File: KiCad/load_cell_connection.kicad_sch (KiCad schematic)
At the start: 10 parts, among them J2 Conn_01x04

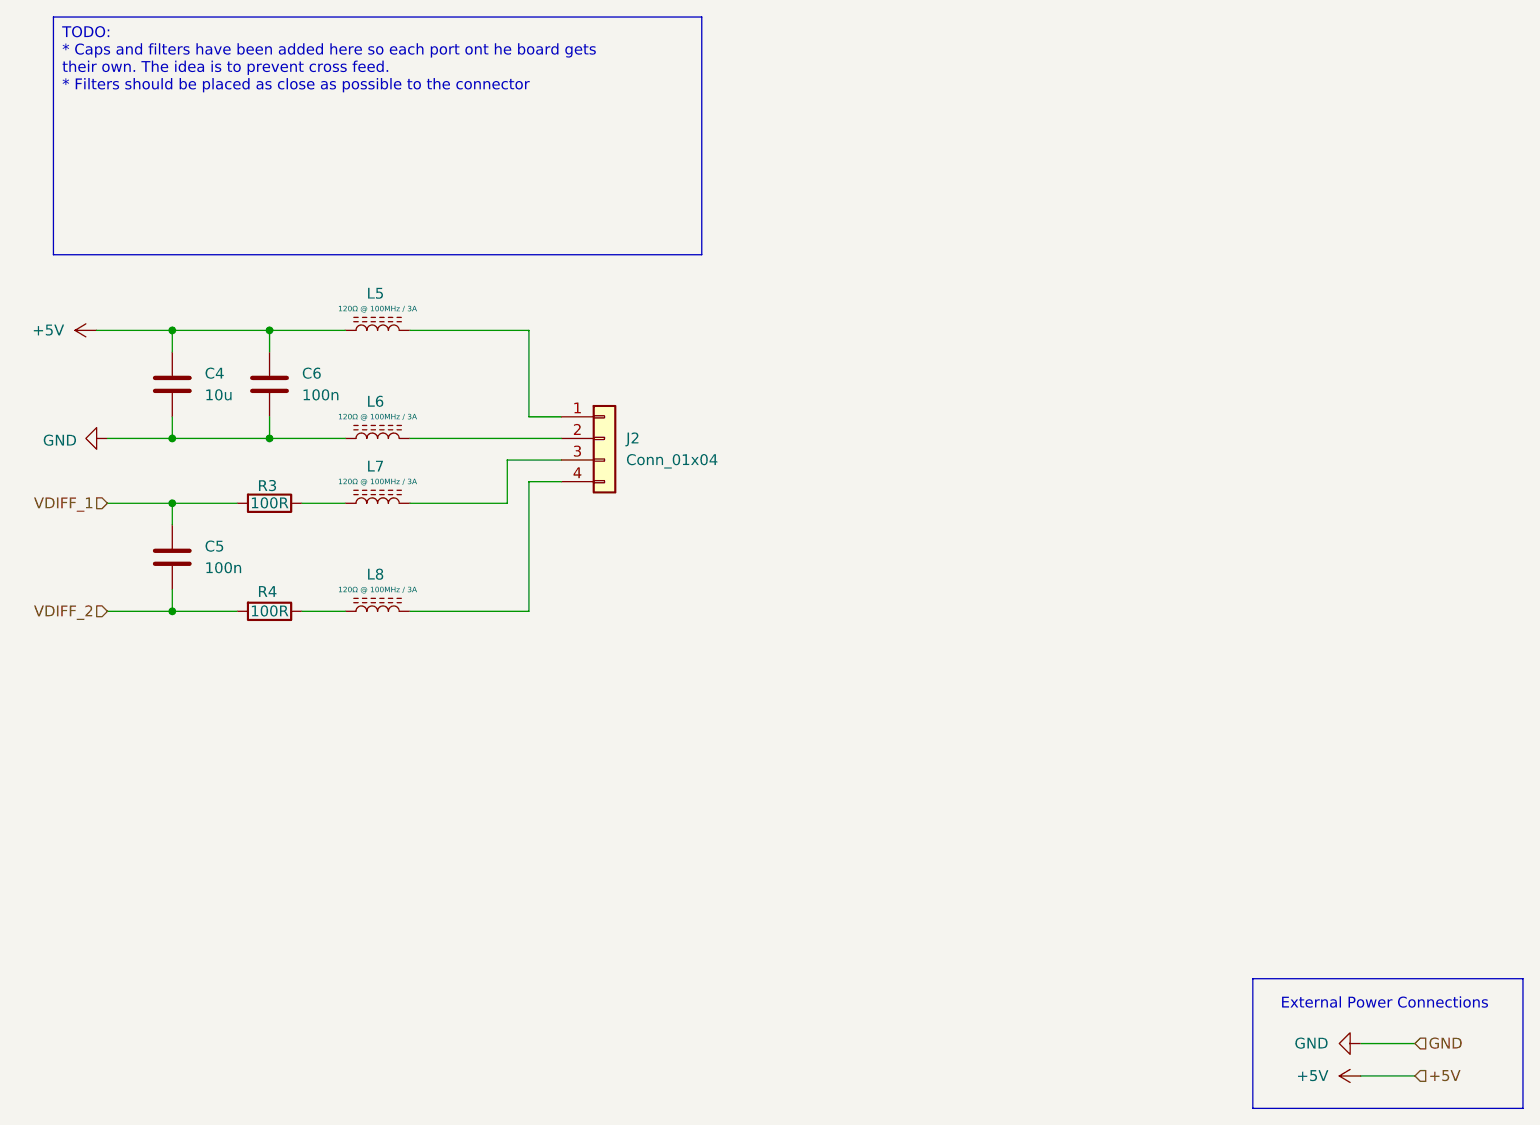
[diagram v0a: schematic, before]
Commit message: Use 12V Power
* Use 12 V Power
* Update to an F103 processor with better compatibility with Katapult
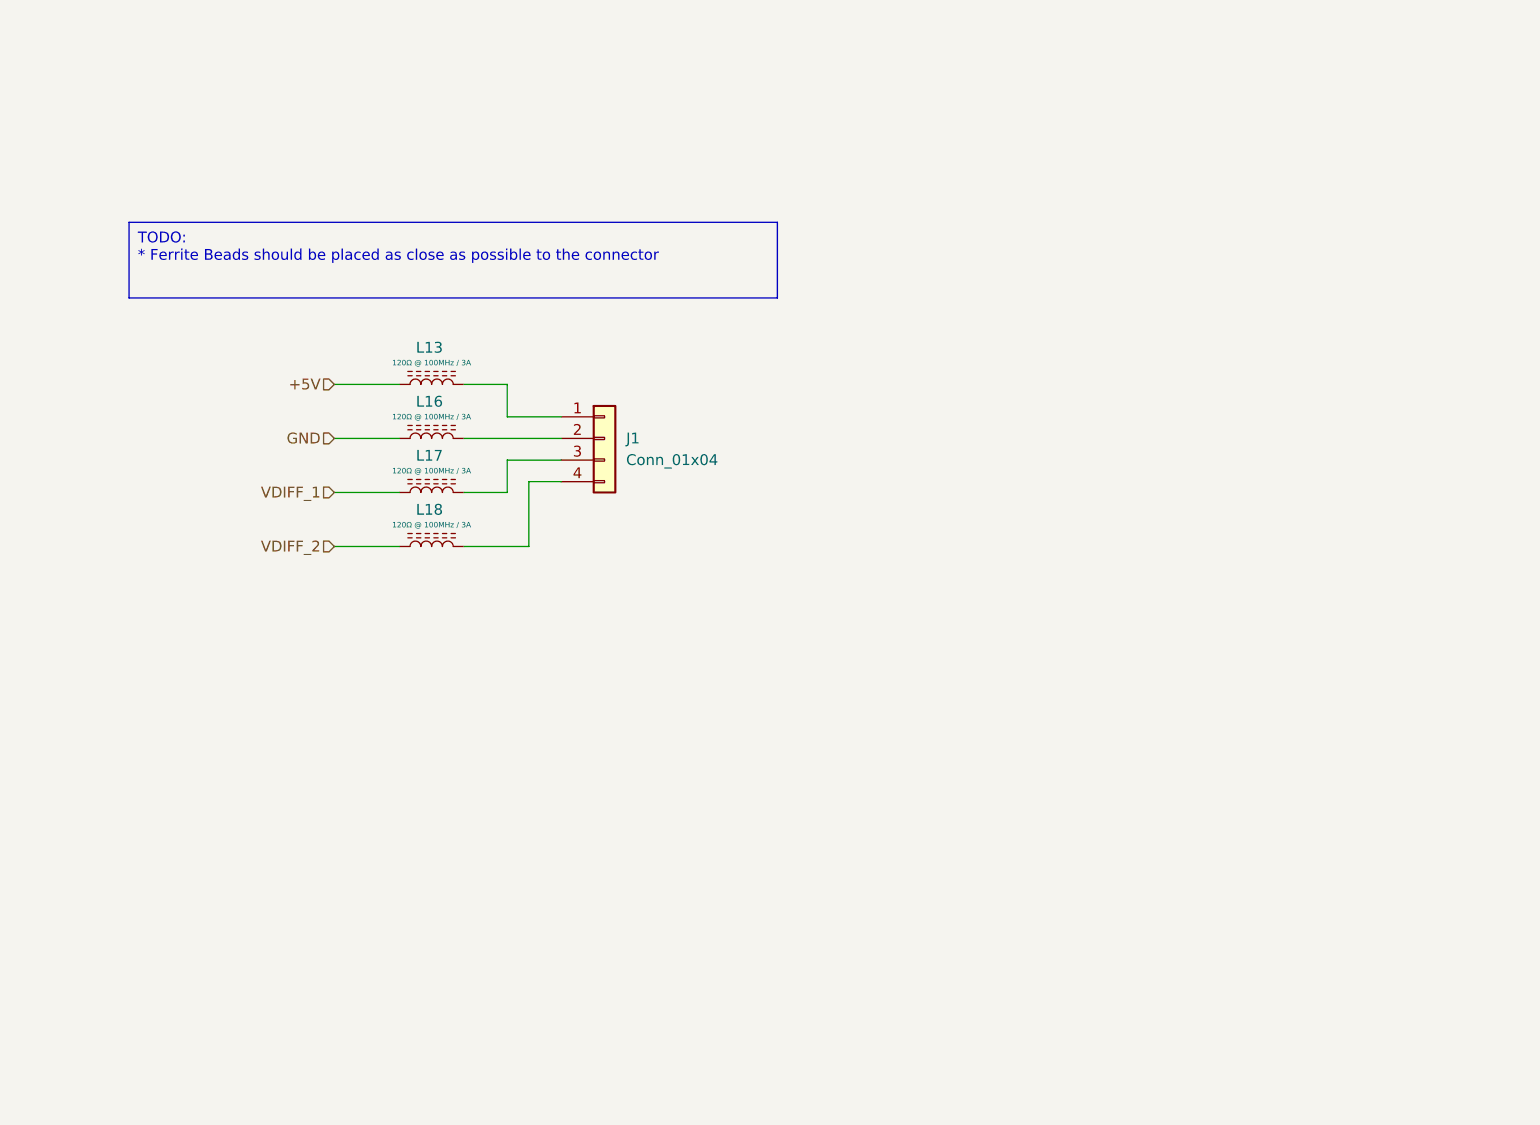
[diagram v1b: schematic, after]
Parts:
- removed C4: 10u, symbol Device:C
- removed C5, C6: 100n, symbol Device:C
- removed R3, R4: 100R, symbol Device:R
- J1: renamed from J2; footprint (none) -> Connector_JST:JST_XH_S4B-XH-A-1_1x04_P2.50mm_Horizontal
- L13: renamed from L5; footprint (none) -> Inductor_SMD:L_0603_1608Metric_Pad1.05x0.95mm_HandSolder
- L16: renamed from L6; footprint (none) -> Inductor_SMD:L_0603_1608Metric_Pad1.05x0.95mm_HandSolder
- L17: renamed from L7; footprint (none) -> Inductor_SMD:L_0603_1608Metric_Pad1.05x0.95mm_HandSolder
- L18: renamed from L8; footprint (none) -> Inductor_SMD:L_0603_1608Metric_Pad1.05x0.95mm_HandSolder
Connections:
- net VDIFF_1: now also L17.1
- net VDIFF_2: now also L18.1
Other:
- note removed: "External Power Connections"
- moved on the sheet: L13, L16, L17, L18

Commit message: Update 5V Power Stage
* Update the 5V power stage based on the recommendations from TI.
* Updated standard passive footprint to 0805 hand solder configuration
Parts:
- L13, L16, L17, L18: footprint Inductor_SMD:L_0603_1608Metric_Pad1.05x0.95mm_HandSolder -> Inductor_SMD:L_0805_2012Metric_Pad1.05x1.20mm_HandSolder
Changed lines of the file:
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@@
 			)
 		)
-		(property "Footprint" "Inductor_SMD:L_0603_1608Metric_Pad1.05x0.95mm_HandSolder"
+		(property "Footprint" "Inductor_SMD:L_0805_2012Metric_Pad1.05x1.20mm_HandSolder"
 			(at 153.67 97.79 0)
 			(effects
@@
 			)
 		)
-		(property "Footprint" "Inductor_SMD:L_0603_1608Metric_Pad1.05x0.95mm_HandSolder"
+		(property "Footprint" "Inductor_SMD:L_0805_2012Metric_Pad1.05x1.20mm_HandSolder"
 			(at 153.67 78.74 0)
 			(effects
@@
 			)
 		)
-		(property "Footprint" "Inductor_SMD:L_0603_1608Metric_Pad1.05x0.95mm_HandSolder"
+		(property "Footprint" "Inductor_SMD:L_0805_2012Metric_Pad1.05x1.20mm_HandSolder"
 			(at 153.67 91.44 0)
 			(effects
@@
 			)
 		)
-		(property "Footprint" "Inductor_SMD:L_0603_1608Metric_Pad1.05x0.95mm_HandSolder"
+		(property "Footprint" "Inductor_SMD:L_0805_2012Metric_Pad1.05x1.20mm_HandSolder"
 			(at 153.67 85.09 0)
 			(effects

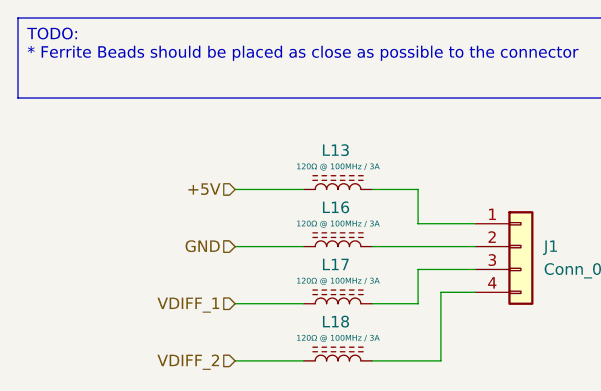
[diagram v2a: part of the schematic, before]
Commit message: Initial Routing
Taking a first pass at layout of the PCB
* load cell connectors were moved to the root schematic and placed on a bus to facilitate PCB routing
* Nets for the filters were directly connected to remove the confusion about GND verses REFN
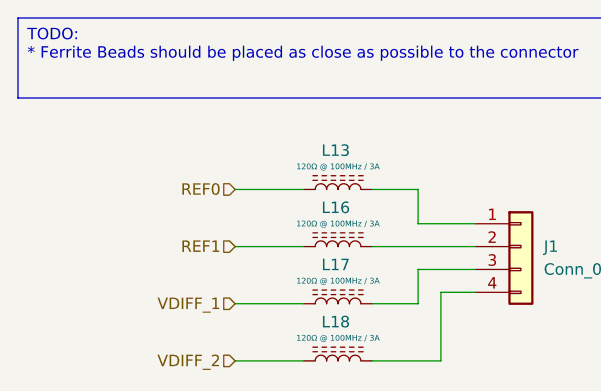
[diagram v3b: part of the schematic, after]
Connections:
- net +5V renamed REF0
- net GND renamed REF1
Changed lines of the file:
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@@
 		)
 	)
-	(hierarchical_label "+5V"
+	(hierarchical_label "REF0"
 		(shape input)
 		(at 142.24 78.74 180)
@@
 		)
 	)
-	(hierarchical_label "GND"
+	(hierarchical_label "REF1"
 		(shape input)
 		(at 142.24 85.09 180)
